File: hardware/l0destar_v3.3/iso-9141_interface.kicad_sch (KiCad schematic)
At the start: 17 parts

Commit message: schematic<>readme discrepency fixes
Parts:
- S10C1: Manufacturer_Name Taiyo Yuden -> Murata; Manufacturer_Part_Number MCASU105SB7104KFNA01 -> GRM155R71H104KE14D
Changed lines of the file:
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@@
 			)
 		)
-		(property "Datasheet" "https://ds.yuden.co.jp/TYCOMPAS/or/detail?pn=MCASU105SB7104KFNA01&u=M"
+		(property "Datasheet" ""
 			(at 165.1 40.64 0)
 			(hide yes)
@@
 			)
 		)
-		(property "Description" "Unpolarized capacitor"
+		(property "Description" ""
 			(at 165.1 40.64 0)
 			(hide yes)
@@
 			)
 		)
-		(property "Manufacturer_Part_Number" "MCASU105SB7104KFNA01"
+		(property "Manufacturer_Part_Number" "GRM155R71H104KE14D"
 			(at 165.1 40.64 0)
 			(hide yes)
@@
 			)
 		)
-		(property "Manufacturer_Name" "Taiyo Yuden"
+		(property "Manufacturer_Name" "Murata"
 			(at 165.1 40.64 0)
 			(hide yes)

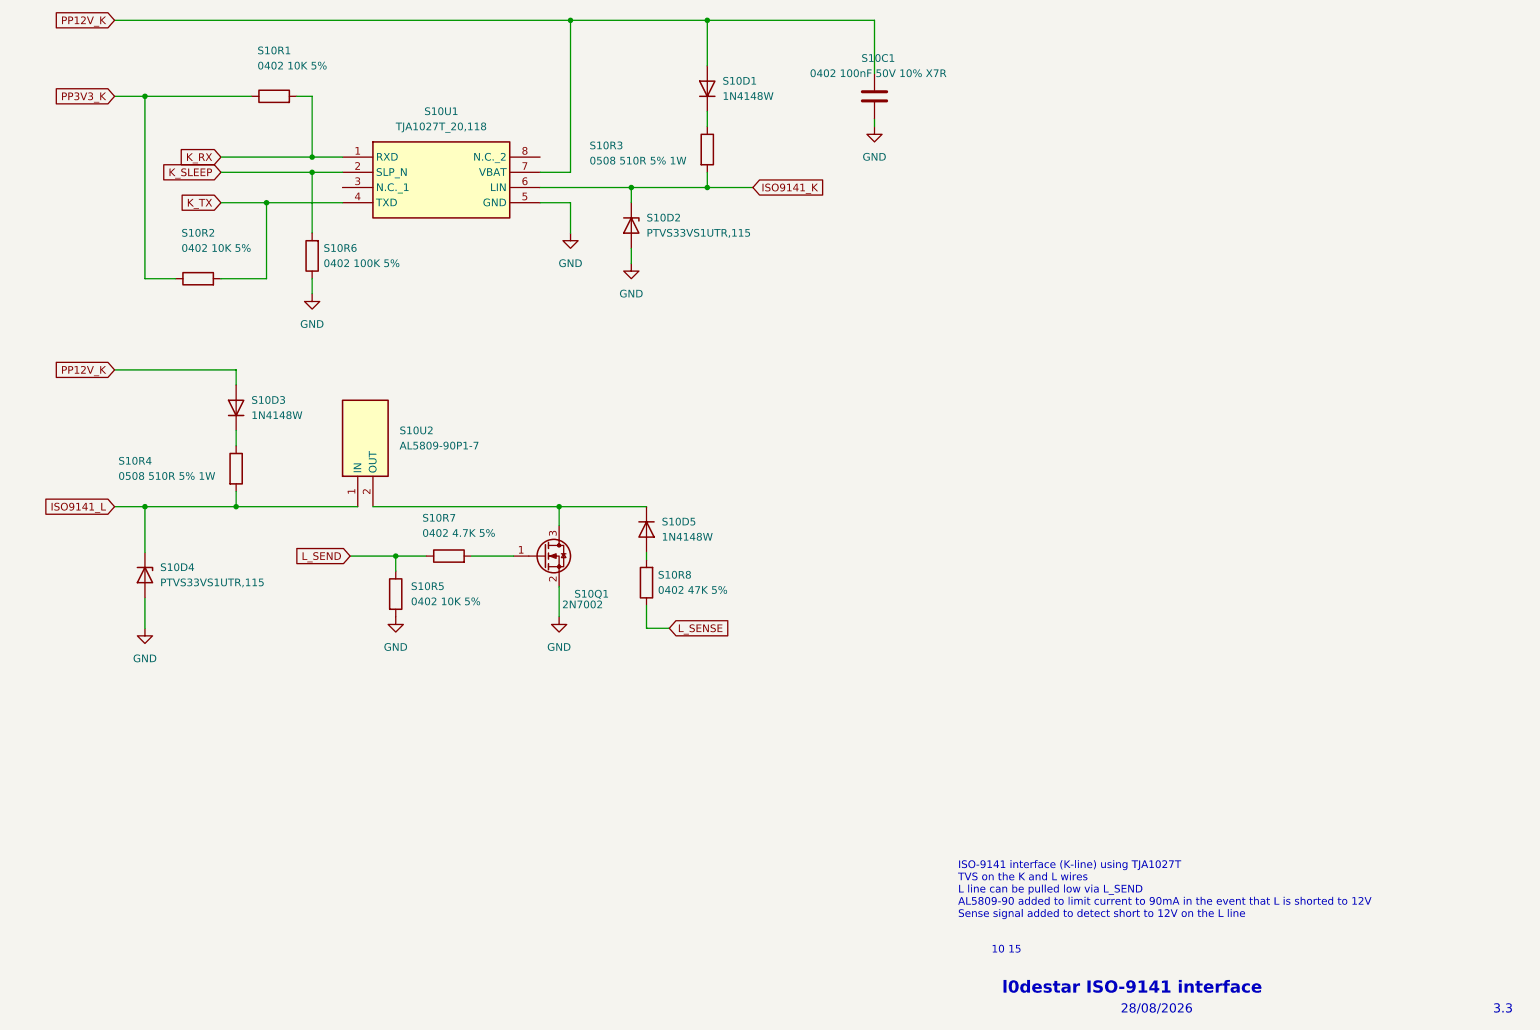
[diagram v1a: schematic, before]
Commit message: revised 3.3 board, parts and readme updates
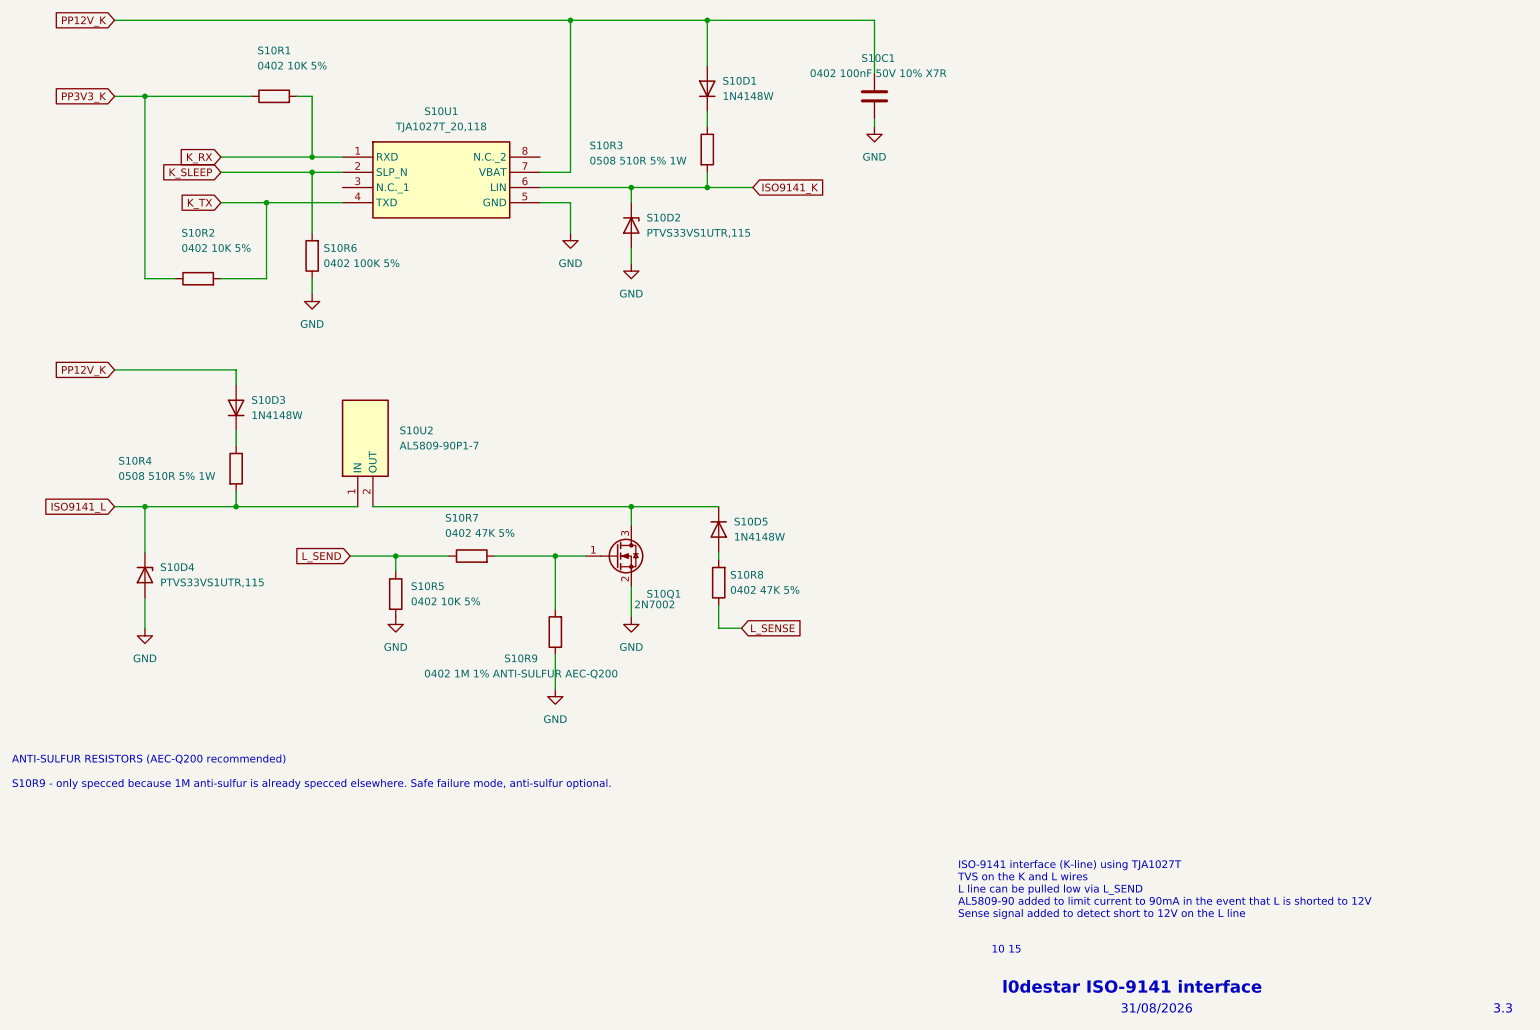
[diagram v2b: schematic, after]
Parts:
- added S10R9: 0402 1M 1% ANTI-SULFUR AEC-Q200, Resistor_SMD:R_0402_1005Metric, symbol Device:R
- S10R7: value 0402 4.7K 5% -> 0402 47K 5%
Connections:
- net GND: now also S10R9.1
- net at S10Q1.1 (G), S10R7.2: now also S10R9.2
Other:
- note added: "31/08/2026"
- note added: "ANTI-SULFUR RESISTORS (AEC-Q200 recommended) S10R9 - only specced because 1M anti-sulfur is already specced elsewhere. Safe failure mode, anti-sulfur optional."
- note removed: "28/08/2026"
- moved on the sheet: S10D5, S10Q1, S10R7, S10R8

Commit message: fixed the 0508 footprint in v3.3 to actually match the part dimensions properly, saving precious microns of board real estate
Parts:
- S10R3, S10R4: footprint Resistor_SMD:R_0508_1220Metric -> libs:R_0508_1220Metric_WideTerminal
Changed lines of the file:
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@@
 			)
 		)
-		(property "Footprint" "Resistor_SMD:R_0508_1220Metric"
+		(property "Footprint" "libs:R_0508_1220Metric_WideTerminal"
 			(at 135.382 49.53 90)
 			(hide yes)
@@
 			)
 		)
-		(property "Footprint" "Resistor_SMD:R_0508_1220Metric"
+		(property "Footprint" "libs:R_0508_1220Metric_WideTerminal"
 			(at 56.642 102.87 90)
 			(hide yes)
